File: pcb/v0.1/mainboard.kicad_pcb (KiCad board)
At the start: 4 copper layers, 156.4 x 94.8 mm, 124 parts, among them J1 Conn_01x02_Pin, J11 Conn_01x03_Pin, J12 Conn_02x08_Odd_Even, J13 Conn_02x08_Odd_Even, J2 TYPE_C_Receptacle, J3 Conn_01x04_Pin, J4 TYPE_C_Receptacle, J5 TYPE_C_Receptacle, J6 22s_disp_connector, J7 ComputeModule5-CM5_connector, J8 Micro_SD_molex, J9 AudioJack3, Q1 MMBT2222A, SW1 SW_Push_45deg, U1 AP2112K-3.3TRG1, U2 Nexperia PUSB3FR4Z, U3 Nexperia PUSB3FR4Z, U4 PCM5102A, U5 RT9742GGJ5, U6 RT9742GGJ5, U7 MDBT50Q-P1MV2, U8 AP22653W6-7, Y1 O_32.768kHz

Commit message: New rough layout
Had to change everything up due to the requirements of the high speed
lines. The board is now also a lot smaller
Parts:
- moved R4 330.1 mm to (122.0, 57.5), turned to 90 degrees
- moved TP3 327.7 mm to (115.6, 49.5), turned to 90 degrees
- moved R3 326.9 mm to (122.0, 60.7), turned to 90 degrees
- moved C11 324.8 mm to (119.4, 58.2), turned to 90 degrees
- moved FB1 324.6 mm to (115.5, 52.2), turned to -90 degrees
- moved C12 324.1 mm to (116.5, 54.1), turned to 180 degrees
- moved U6 324.1 mm to (112.7, 48.4), turned to 90 degrees
- moved C20 322.9 mm to (117.5, 56.9), turned to -90 degrees
- moved R5 322.4 mm to (120.3, 62.2), turned to 90 degrees
- moved C19 319.7 mm to (112.4, 51.9), turned to 180 degrees
- moved R6 319.6 mm to (118.7, 62.2), turned to 90 degrees
- moved C23 318.9 mm to (109.6, 48.5), turned to 90 degrees
- moved R7 316.8 mm to (117.1, 62.2), turned to 90 degrees
- moved C17 315.6 mm to (111.4, 54.2), turned to 0 degrees
- moved FB2 313.3 mm to (108.7, 52.2), turned to -90 degrees
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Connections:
- J4 pad A5: /HighSpeed/fw_cc1_1 -> /HighSpeed/fw_cc1_0
- J4 pad B5: /HighSpeed/fw_cc2_1 -> /HighSpeed/fw_cc2_0
- R20 pad 2: /HighSpeed/fw_cc1_1 -> /HighSpeed/fw_cc1_0
- R21 pad 2: /HighSpeed/fw_cc2_1 -> /HighSpeed/fw_cc2_0
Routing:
- net /HighSpeed/USB3-1-D_P: track 46.6 -> 48.3 mm
- net /HighSpeed/USB3-1-D_N: track 46.4 -> 47.9 mm
- net /HighSpeed/USB3-0-D_P: track 47.5 -> 48.6 mm
- net /HighSpeed/USB3-0-D_N: track 47.0 -> 48.1 mm
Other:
- board size 156.4 x 94.8 mm -> 129.3 x 88.4 mm

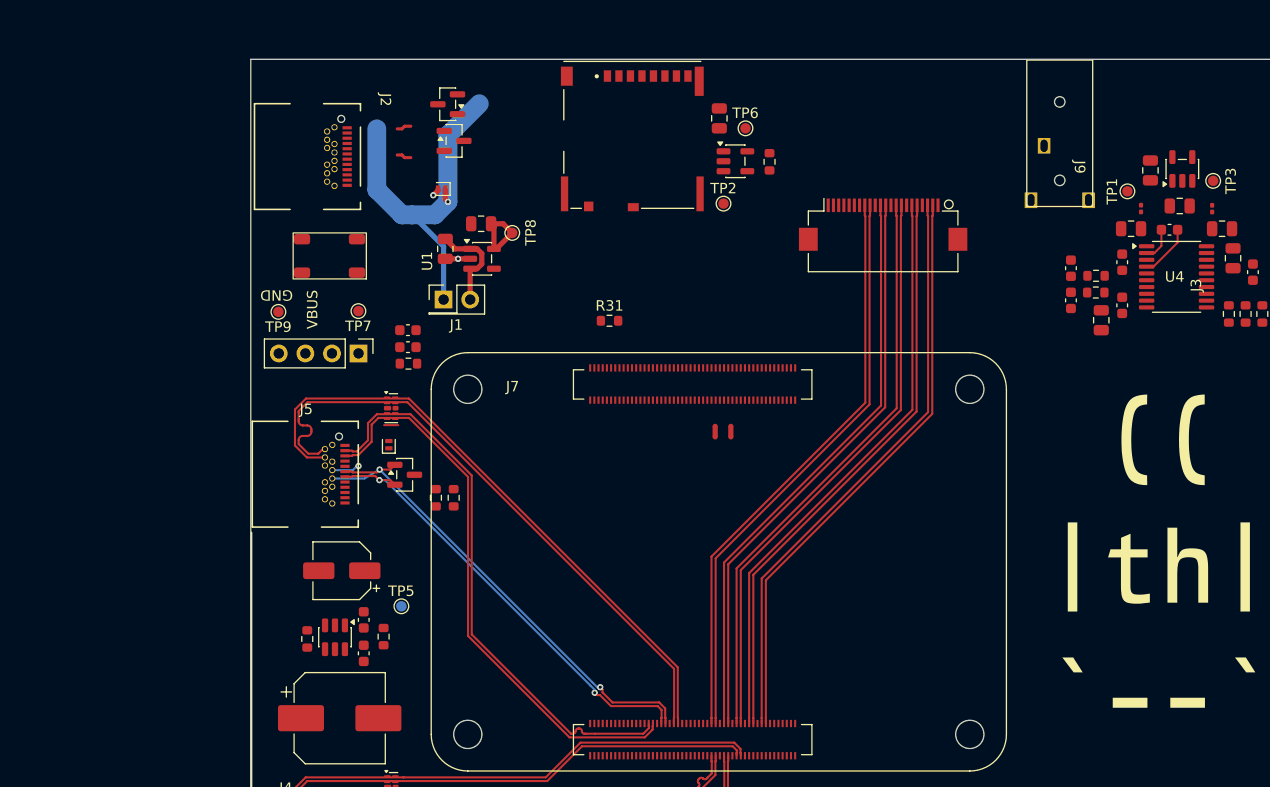
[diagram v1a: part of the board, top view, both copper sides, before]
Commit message: High power routing
Finished the single high power line. It should be able to hold peaks of
5A without heating up too much, but only testing will reveal.
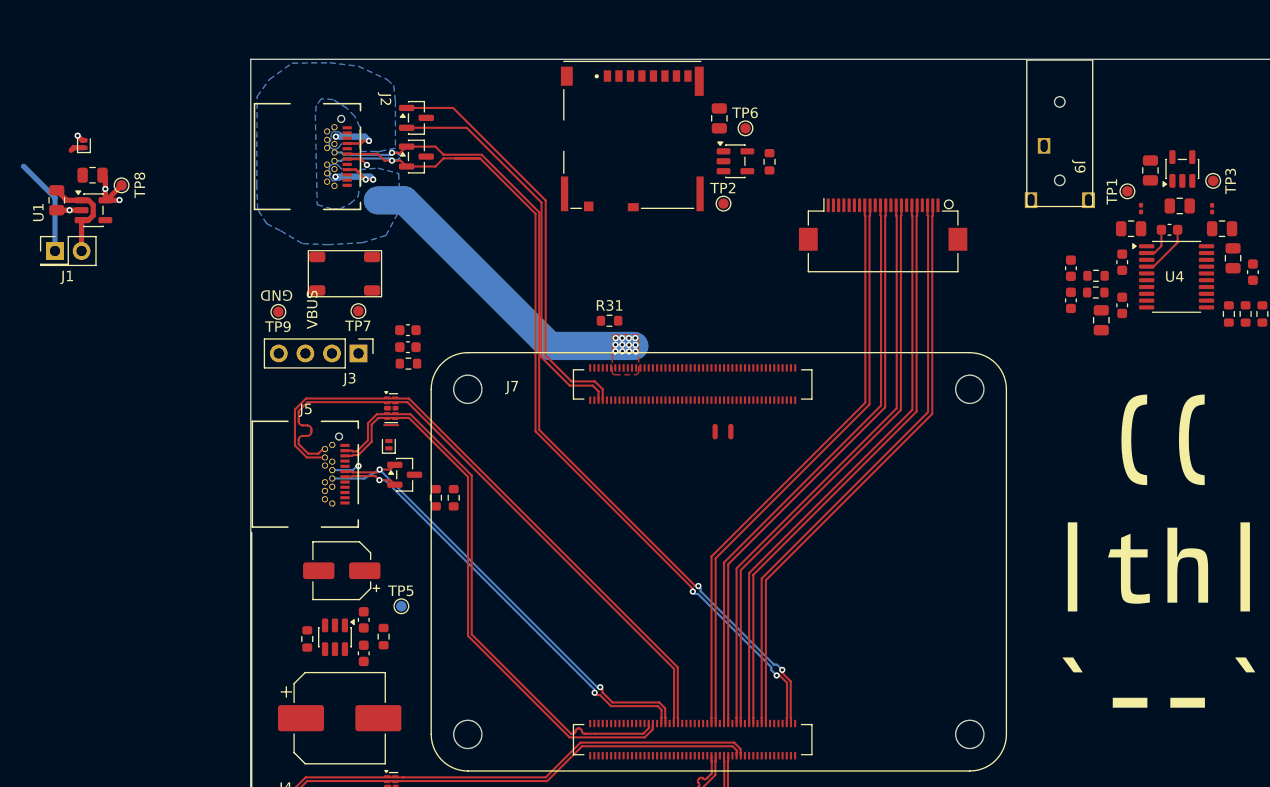
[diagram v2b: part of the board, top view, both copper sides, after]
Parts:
- moved TP8 37.6 mm to (11.2, 50.0)
- moved C1 37.4 mm to (5.04, 51.4)
- moved C2 37.4 mm to (8.47, 49.0)
- moved U1 37.4 mm to (8.56, 52.3)
- moved J1 37.4 mm to (4.88, 56.2)
- moved D22 34.5 mm to (7.64, 46.0), turned to 90 degrees
- moved D4 3.90 mm to (39.4, 47.2)
- moved D5 3.26 mm to (39.4, 43.5), turned to 0 degrees
- moved SW1 2.23 mm to (32.6, 58.4)
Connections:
- D4 pad 1: /USB2_P -> /USB2_N
- D4 pad 2: /USB2_N -> /USB2_P
- D5 pad 1: /USB2_CC2 -> /USB2_CC1
- D5 pad 2: /USB2_CC1 -> /USB2_CC2
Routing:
- net /USB2_P: track 0.00 -> 88.9 mm, vias 0 -> 3
- net /USB2_N: track 0.00 -> 87.6 mm, vias 0 -> 4
- net /USB2_CC1: track 0.00 -> 39.9 mm
- net /USB2_CC2: track 0.00 -> 38.4 mm
- net /+5v: track 38.2 -> 53.1 mm, vias 1 -> 17
- net /+3v3_LDO: track 9.54 -> 8.27 mm, vias 0 -> 2
- added copper zone on B.Cu, net /+5v
- added copper zone on F.Cu, net /+5v
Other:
- rule pad_to_mask_clearance: 0.1 -> 0.05
- rule solder_mask_min_width: 0.3 -> 0.2

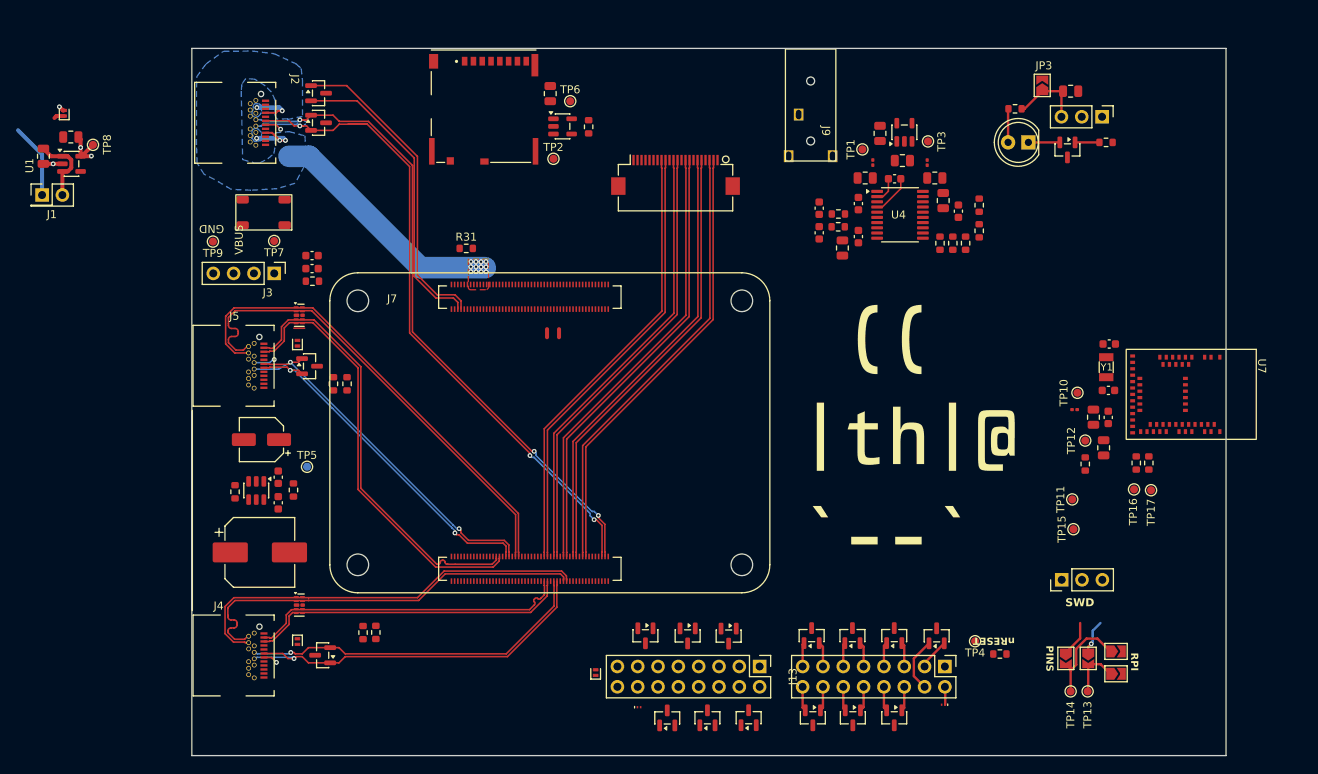
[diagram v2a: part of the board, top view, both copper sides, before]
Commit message: A large chunk of the pcb routing + shrinking the board
Did a large chunk of the PCB routing, probably just under half of all
remaining traces. Additionally I shrank the pcb to below 100x100 as it
reduces the price of manufacturing by roughly 4x
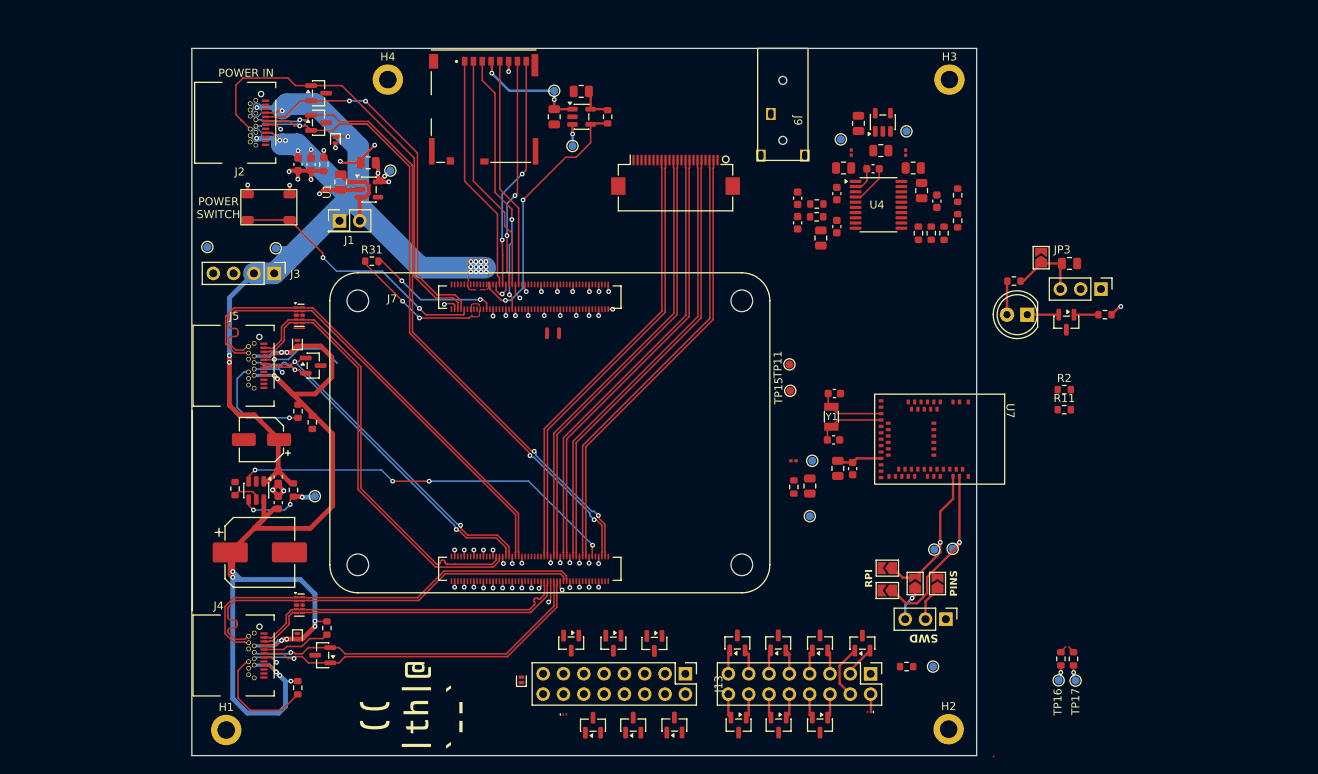
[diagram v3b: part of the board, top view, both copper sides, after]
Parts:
- added C5: 10uf, Capacitor_SMD:C_0805_2012Metric, F.Cu at (72.3, 43.3)
- added H1: MountingHole_Pad, MountingHole:MountingHole_2.2mm_M2_DIN965_Pad, F.Cu at (27.9, 123.1)
- added H2: MountingHole_Pad, MountingHole:MountingHole_2.2mm_M2_DIN965_Pad, F.Cu at (118.2, 123.0)
- added H3: MountingHole_Pad, MountingHole:MountingHole_2.2mm_M2_DIN965_Pad, F.Cu at (118.3, 41.8)
- added H4: MountingHole_Pad, MountingHole:MountingHole_2.2mm_M2_DIN965_Pad, F.Cu at (48.1, 41.8)
- added R11: 100k, Resistor_SMD:R_0603_1608Metric, F.Cu at (132.7, 83.1)
- added R2: 1k, Resistor_SMD:R_0603_1608Metric, F.Cu at (132.7, 80.6)
- moved TP15 39.4 mm to (98.4, 80.7)
- moved TP11 39.2 mm to (98.3, 77.4)
- moved C2 37.3 mm to (45.6, 52.2)
- moved TP8 37.3 mm to (48.4, 53.2)
- moved U1 37.3 mm to (45.7, 55.5)
- moved C1 37.3 mm to (42.2, 54.6)
- moved J1 37.3 mm to (42.1, 59.5)
- moved C24 37.0 mm to (100.8, 92.6), turned to 90 degrees
- moved R12 36.5 mm to (98.8, 92.7), turned to 90 degrees
- moved FB3 35.7 mm to (98.8, 89.5)
- moved TP12 35.7 mm to (100.8, 96.4)
- moved C27 34.9 mm to (103.8, 86.8)
- moved C28 34.9 mm to (103.9, 81.0)
- moved Y1 34.9 mm to (103.5, 83.9)
- moved TP10 34.2 mm to (101.2, 89.5)
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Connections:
- net Net-(U7A-D+) renamed /Co processor/nRF_USB_P
- net Net-(U7A-D-) renamed /Co processor/nRF_USB_N
- D5 pad 1: /USB2_CC1 -> /USB2_CC2
- D5 pad 2: /USB2_CC2 -> /USB2_CC1
- R21 pad 1: unconnected-(R21-Pad1) -> /HighSpeed/FW_VBUS
- U7 pad 7: unconnected-(U7A-P1.14_LF-Pad7) -> /Co processor/MOD4
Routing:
- net /HighSpeed/FW_VBUS: track 0.00 -> 142.7 mm, vias 0 -> 13
- net GND: track 3.16 -> 74.5 mm, vias 2 -> 62
- net /+5v: track 53.1 -> 121.8 mm, vias 17 -> 23
- net /HighSpeed/VBUS_EN: track 0.00 -> 49.3 mm, vias 0 -> 4
- net /GPIO/PWR_BUT: track 0.00 -> 32.9 mm, vias 0 -> 2
- net /GPIO/SD_PWR_ON: track 0.00 -> 32.8 mm, vias 0 -> 2
- net /GPIO/SD_CMD: track 0.00 -> 32.8 mm, vias 0 -> 2
- net /GPIO/SD_DAT3: track 0.00 -> 29.9 mm
- net /GPIO/SD_DAT2: track 0.00 -> 29.7 mm
- net /GPIO/SD_DAT1: track 0.00 -> 29.2 mm, vias 0 -> 2
- net /GPIO/SD_CLK: track 0.00 -> 28.9 mm
- net /GPIO/SD_DAT0: track 0.00 -> 28.6 mm, vias 0 -> 2
- net /+3v3_PI: track 0.00 -> 21.1 mm, vias 0 -> 2
- net /USB2_CC2: track 38.4 -> 55.6 mm
- net /GPIO/GPIO_VREF: track 0.00 -> 17.0 mm, vias 0 -> 2
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- added copper zone on F.Cu, net /+3v3_PI
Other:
- board size 129.3 x 88.4 mm -> 98.1 x 88.4 mm
- board text added: "+5v"
- board text added: "CLK"
- board text added: "DIO"
- board text added: "POWER IN"
- board text added: "POWER SWITCH"
- board text removed: "VBUS"

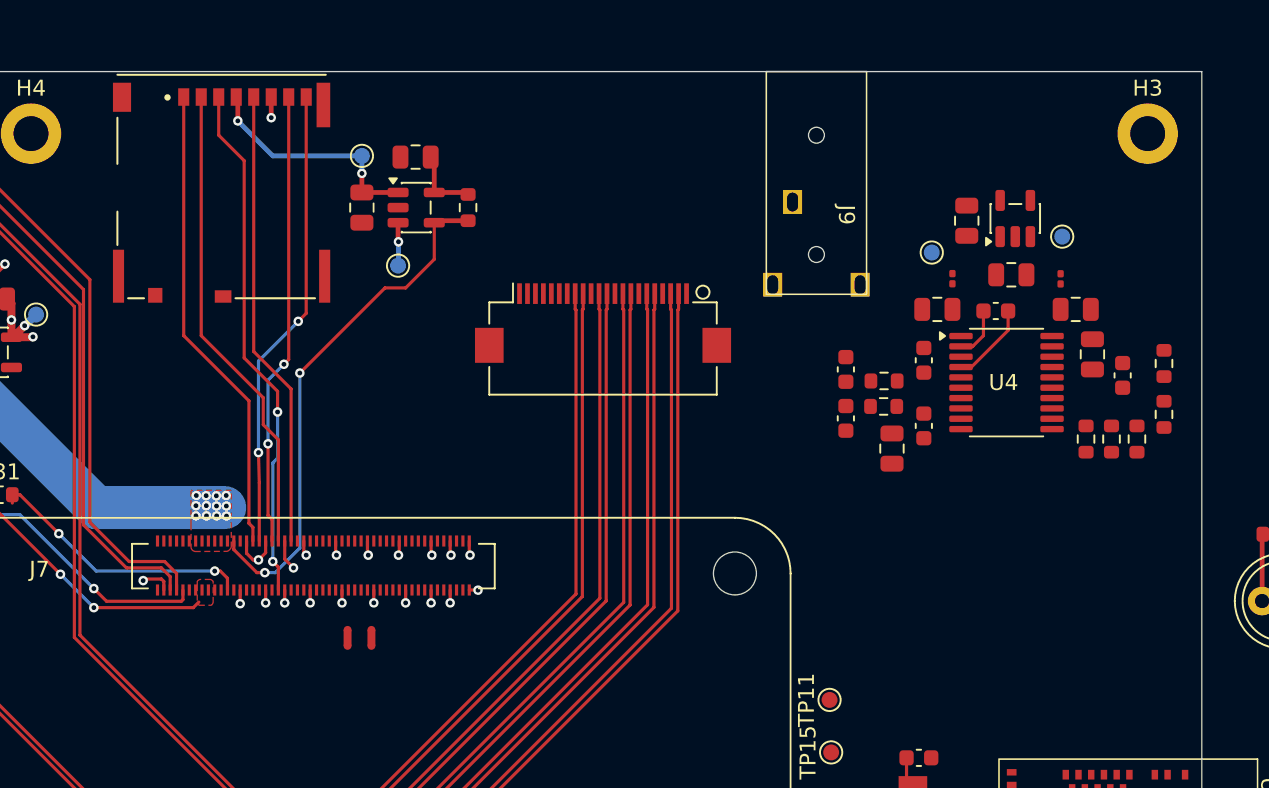
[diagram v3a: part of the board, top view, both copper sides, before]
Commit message: Working on GPIO lines of the cm5
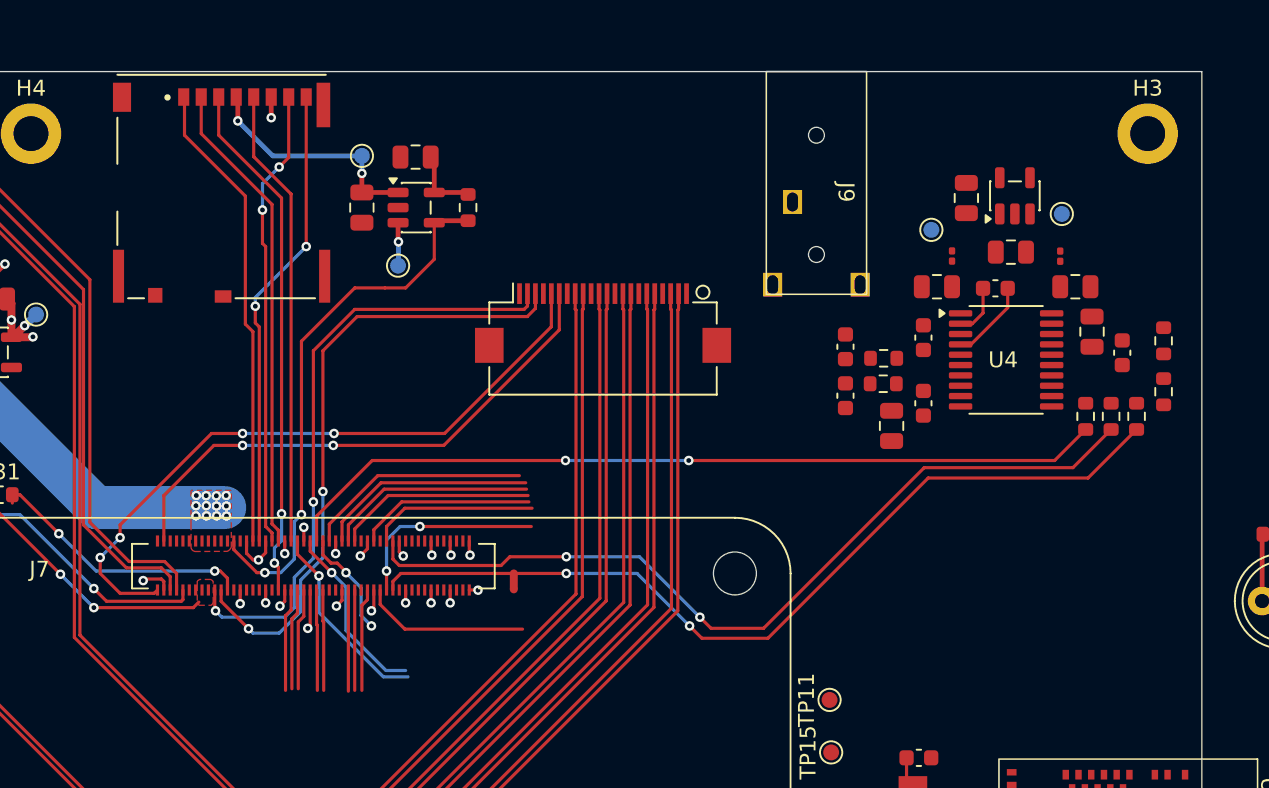
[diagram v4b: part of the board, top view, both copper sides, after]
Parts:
- removed NT1: NetTie_2, NetTie:NetTie-2_SMD_Pad0.5mm
- moved NT2 9.63 mm to (78.5, 70.0), turned to -90 degrees
- moved C12 1.43 mm to (113.8, 51.4)
- moved C14 1.43 mm to (105.0, 51.4)
- moved C17 1.43 mm to (108.7, 51.5)
- moved C22 1.43 mm to (99.3, 58.3)
- moved FB2 1.43 mm to (106.0, 49.5)
- moved R3 1.43 mm to (119.3, 58.0)
- moved R9 1.43 mm to (101.7, 57.5)
- moved C15 1.43 mm to (102.2, 60.2)
- moved R8 1.43 mm to (101.7, 55.9)
- moved U4 1.43 mm to (109.4, 56.0)
- moved U6 1.43 mm to (110.0, 45.7)
- moved C20 1.43 mm to (114.8, 54.2)
- moved C21 1.43 mm to (99.3, 55.2)
- moved FB1 1.43 mm to (112.8, 49.5)
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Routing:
- net /GPIO/I2S_LRCK: track 0.00 -> 54.6 mm, vias 0 -> 2
- net /GPIO/I2S_DIN: track 0.00 -> 53.9 mm, vias 0 -> 2
- net /GPIO/I2S_BCK: track 0.00 -> 52.2 mm, vias 0 -> 2
- net /GPIO/CAM_GPIO1: track 0.00 -> 42.1 mm, vias 0 -> 4
- net /GPIO/SCL0: track 0.00 -> 39.5 mm, vias 0 -> 2
- net /GPIO/SDA0: track 0.00 -> 38.7 mm, vias 0 -> 2
- net /GPIO/CAM_GPIO0: track 0.00 -> 34.0 mm, vias 0 -> 2
- net /Co processor/MOD3: track 0.00 -> 14.3 mm
- net /Co processor/MOD2: track 0.00 -> 13.8 mm
- net /Co processor/MOD1: track 0.00 -> 13.1 mm
- net /Co processor/U1_RX: track 0.00 -> 12.6 mm, vias 0 -> 2
- net /Co processor/MOD0: track 0.00 -> 12.5 mm
- net /Co processor/U0_RX: track 0.00 -> 12.3 mm, vias 0 -> 1
- net /Co processor/U0_TX: track 0.00 -> 11.3 mm, vias 0 -> 1
- net /Co processor/U1_TX: track 0.00 -> 11.2 mm
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
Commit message: Finish CM5 GPIO pinout (including DAC pins)
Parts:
- added NT1: NetTie_2, NetTie:NetTie-2_SMD_Pad0.5mm, F.Cu at (96.5, 62.9)
- moved NT2 18.3 mm to (96.7, 71.7)
- moved TP11 4.64 mm to (101.1, 73.7)
- moved TP15 4.26 mm to (101.1, 77.4)
- moved D18 0.28 mm to (71.3, 112.2)
- moved D14 0.20 mm to (79.0, 122.5)
- moved D13 0.10 mm to (84.0, 122.5)
- moved D15 0.10 mm to (73.8, 122.5)
- moved D16 0.10 mm to (81.5, 112.3)
- moved D17 0.10 mm to (76.4, 112.3)
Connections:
- D14 pad 1: /GPIO/GP03/I2C1_SCL -> /GPIO/GP9
- D14 pad 2: /GPIO/GP23/I2S_DIN1 -> /GPIO/GP11/I2C1_SCL
- D15 pad 1: /GPIO/GP9 -> /GPIO/GP03/I2C1_SCL
- D15 pad 2: /GPIO/GP02/I2C1_SDA -> /GPIO/GP04/CLK0/U2_TX/I2C2_SDA
- D16 pad 1: /GPIO/GP04/CLK0/U2_TX/I2C2_SDA -> /GPIO/GP23/I2S_DIN1
- D18 pad 1: /GPIO/GP11/I2C1_SCL -> /GPIO/GP02/I2C1_SDA
- J13 pad 10: /GPIO/GP02/I2C1_SDA -> /GPIO/GP04/CLK0/U2_TX/I2C2_SDA
- J13 pad 11: /GPIO/GP11/I2C1_SCL -> /GPIO/GP02/I2C1_SDA
- J13 pad 12: /GPIO/GP9 -> /GPIO/GP03/I2C1_SCL
- J13 pad 3: /GPIO/GP04/CLK0/U2_TX/I2C2_SDA -> /GPIO/GP23/I2S_DIN1
- J13 pad 6: /GPIO/GP23/I2S_DIN1 -> /GPIO/GP11/I2C1_SCL
- J13 pad 8: /GPIO/GP03/I2C1_SCL -> /GPIO/GP9
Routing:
- net /+3v3_PI: track 21.1 -> 90.6 mm, vias 2 -> 5
- net /GPIO/GP18/I2S_BCK: track 0.00 -> 67.7 mm, vias 0 -> 2
- net /GPIO/GP19/I2S_LRCK: track 0.00 -> 58.5 mm, vias 0 -> 3
- net /GPIO/GP04/CLK0/U2_TX/I2C2_SDA: track 6.35 -> 61.8 mm, vias 0 -> 3
- net /GPIO/GP03/I2C1_SCL: track 6.35 -> 61.5 mm, vias 0 -> 2
- net /GPIO/GP11/I2C1_SCL: track 6.31 -> 59.6 mm, vias 0 -> 3
- net /GPIO/GP9: track 6.36 -> 59.5 mm, vias 0 -> 2
- net /GPIO/GP02/I2C1_SDA: track 6.45 -> 55.7 mm, vias 0 -> 2
- net /GPIO/GP23/I2S_DIN1: track 6.83 -> 55.7 mm, vias 2 -> 4
- net /GPIO/GP17: track 6.33 -> 52.9 mm, vias 0 -> 2
- net /GPIO/GP27: track 6.33 -> 52.3 mm, vias 0 -> 2
- net /GPIO/GP05/CLK2/U2_RX/I2C2_SCL: track 6.45 -> 51.1 mm, vias 0 -> 2
- net /Co processor/U0_TX: track 11.3 -> 37.5 mm, vias 1 -> 2
- net /Co processor/U0_RX: track 12.3 -> 37.7 mm, vias 1 -> 2
